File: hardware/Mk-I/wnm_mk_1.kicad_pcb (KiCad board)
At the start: 2 copper layers, 96.5 x 66 mm, 122 parts, among them CON1 USB-MICRO-B, SW1 SW_PUSH, SW10 SW_PUSH, SW11 SW_PUSH, SW12 SW_PUSH, SW13 SW_PUSH, SW14 SW_PUSH, SW15 SW_PUSH, SW16 SW_PUSH, SW18 SW_PUSH, SW19 SW_PUSH, SW2 SW_PUSH, SW20 SW_PUSH, SW21 SW_PUSH, SW22 SW_PUSH, SW3 SW_PUSH, SW4 SW_PUSH, SW5 SW_PUSH, SW6 SW_PUSH, SW7 SW_PUSH, SW8 SW_PUSH, SW9 SW_PUSH, U10 STM32_SWD_Connector, U2 MCP73831, U3 BD33IA5, U4 STM32F407VG, U5 SGTL5000, U6 encoder_and_switch, U7 encoder_and_switch, U8 MOLEX_microSD_47219-2001, U9 SSD1306, X1 CRYSTAL

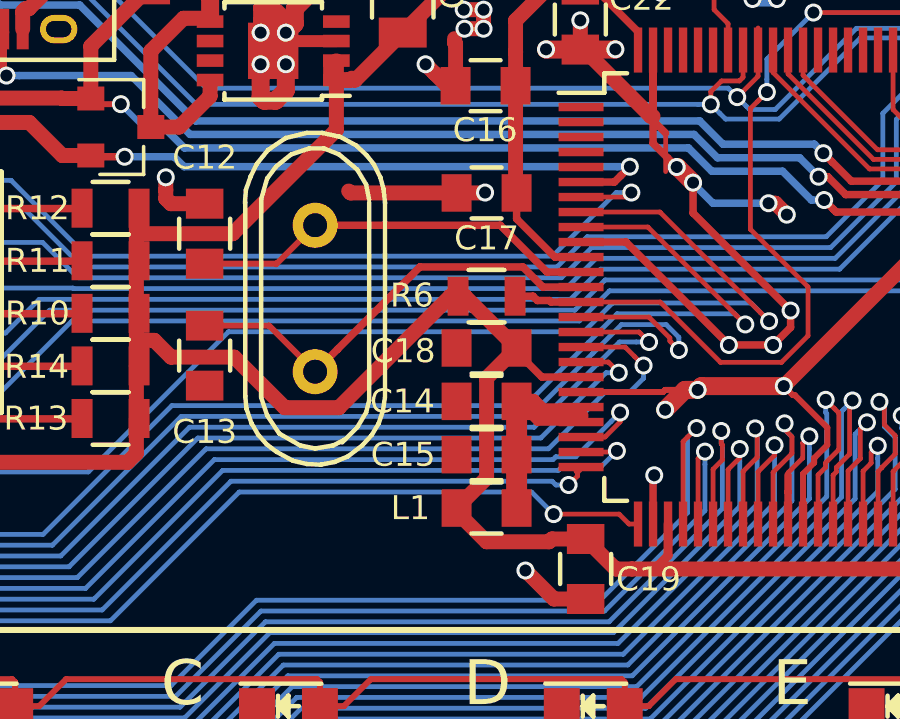
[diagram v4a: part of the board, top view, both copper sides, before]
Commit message: Fix exposed crystal trace by R6 pad mask
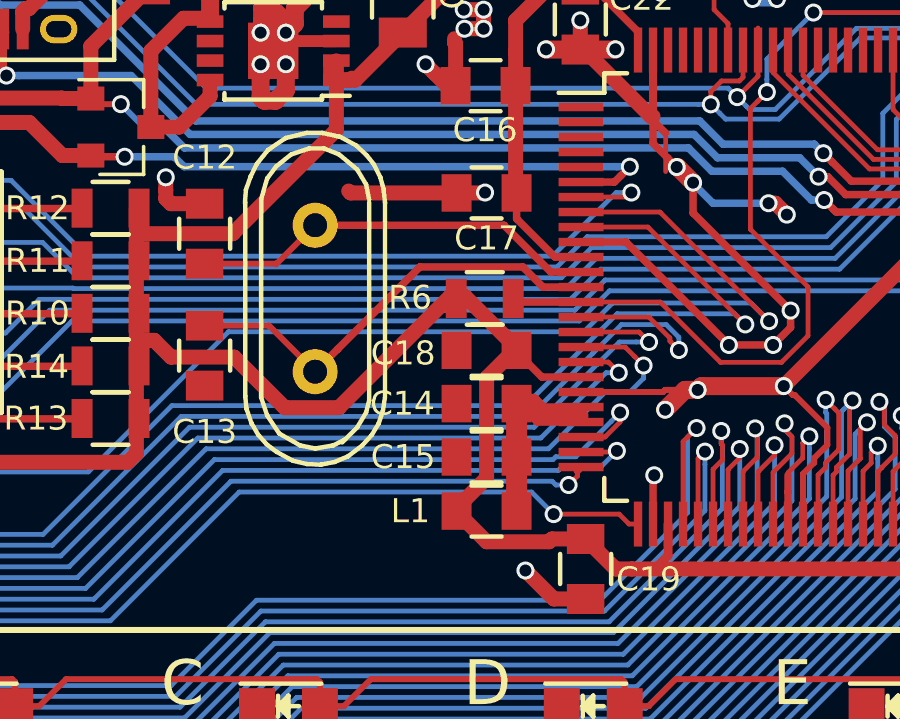
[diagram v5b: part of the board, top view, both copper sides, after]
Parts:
- moved L1 0.10 mm to (145.0, 100.2)
- moved R6 0.10 mm to (145.0, 93.1)
- moved C14 0.08 mm to (145.0, 96.6)
- moved C15 0.08 mm to (145.0, 98.4)
- moved C18 0.08 mm to (145.0, 94.8)
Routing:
- net GND: track 159.0 -> 157.0 mm, vias 56 -> 52
- net (no net): track 0.00 -> 1.93 mm, vias 0 -> 4
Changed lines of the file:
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@@
   (general
     (links 336)
-    (no_connects 1)
+    (no_connects 0)
     (area 79.934999 78.664999 176.605001 144.855001)
     (thickness 1.6)
     (drawings 96)
-    (tracks 2008)
+    (tracks 2005)
     (zones 0)
     (modules 122)
@@
   )
   (setup
-    (last_trace_width 0.5)
+    (last_trace_width 0.25)
     (user_trace_width 0.16)
     (user_trace_width 0.2)
@@
   )
   (module Capacitors_SMD:C_0805 (layer F.Cu)
-    (at 145.034 96.52)
+    (at 145.034 96.5962)
     (descr "Capacitor SMD 0805, reflow soldering, AVX (see smccp.pdf)")
     (tags "capacitor 0805")
@@
   )
   (module Capacitors_SMD:C_0805 (layer F.Cu)
-    (at 145.034 98.298)
+    (at 145.034 98.3742)
     (descr "Capacitor SMD 0805, reflow soldering, AVX (see smccp.pdf)")
     (tags "capacitor 0805")
@@
   )
   (module Capacitors_SMD:C_0805 (layer F.Cu)
-    (at 145.034 94.742)
+    (at 145.034 94.8182)
     (descr "Capacitor SMD 0805, reflow soldering, AVX (see smccp.pdf)")
     (tags "capacitor 0805")
@@
   )
   (module Capacitors_SMD:C_0805 (layer F.Cu)
-    (at 145.034 100.076)
+    (at 145.034 100.1776)
     (descr "Capacitor SMD 0805, reflow soldering, AVX (see smccp.pdf)")
     (tags "capacitor 0805")
@@
   )
   (module Resistors_SMD:R_0805 (layer F.Cu)
-    (at 145.034 93.0148 180)
+    (at 144.973 93.091 180)
     (descr "Resistor SMD 0805, reflow soldering, Vishay (see dcrcw.pdf)")
     (tags "resistor 0805")
@@
     (effects (font (size 1.5 1.5) (thickness 0.3)))
   )
+  (segment (start 144.9324 84.0994) (end 144.2974 84.0994) (width 0.5) (layer F.Cu) (net 0))
+  (via (at 144.2974 84.0994) (size 0.6) (drill 0.4) (layers F.Cu B.Cu) (net 0))
+  (segment (start 144.9324 83.4644) (end 144.9324 84.0994) (width 0.5) (layer F.Cu) (net 0))
+  (via (at 144.9324 84.0994) (size 0.6) (drill 0.4) (layers F.Cu B.Cu) (net 0))
+  (segment (start 144.9324 83.4644) (end 144.272 83.4644) (width 0.5) (layer F.Cu) (net 0))
+  (via (at 144.272 83.4644) (size 0.6) (drill 0.4) (layers F.Cu B.Cu) (net 0))
+  (via (at 144.9324 83.4644) (size 0.6) (drill 0.4) (layers F.Cu B.Cu) (net 0))
   (segment (start 86.512398 109.47118) (end 95.820601 100.162977) (width 0.16) (layer B.Cu) (net 1))
   (segment (start 95.820601 100.162977) (end 107.7535 100.162977) (width 0.16) (layer B.Cu) (net 1))
@@
   (via (at 87.20819 121.1834) (size 0.6) (drill 0.4) (layers F.Cu B.Cu) (net 30))
   (segment (start 90.505 121.19) (end 84.755 121.19) (width 0.25) (layer F.Cu) (net 30))
-  (segment (start 144.9324 84.0994) (end 144.2974 84.0994) (width 0.5) (layer F.Cu) (net 31))
-  (via (at 144.2974 84.0994) (size 0.6) (drill 0.4) (layers F.Cu B.Cu) (net 31))
-  (segment (start 144.9324 83.4644) (end 144.9324 84.0994) (width 0.5) (layer F.Cu) (net 31))
-  (via (at 144.9324 84.0994) (size 0.6) (drill 0.4) (layers F.Cu B.Cu) (net 31))
-  (segment (start 144.9324 83.4644) (end 144.272 83.4644) (width 0.5) (layer F.Cu) (net 31))
-  (via (at 144.272 83.4644) (size 0.6) (drill 0.4) (layers F.Cu B.Cu) (net 31))
   (segment (start 143.9672 84.5693) (end 143.9672 84.4296) (width 0.5) (layer F.Cu) (net 31))
-  (via (at 144.9324 83.4644) (size 0.6) (drill 0.4) (layers F.Cu B.Cu) (net 31))
   (segment (start 154.432 89.916) (end 154.6606 89.916) (width 0.5) (layer F.Cu) (net 31))
   (segment (start 154.6606 89.916) (end 155.0416 90.297) (width 0.5) (layer F.Cu) (net 31))
@@
   (segment (start 134.792 87.376) (end 135.817 86.351) (width 0.5) (layer F.Cu) (net 42))
   (segment (start 135.817 86.351) (end 135.817 85.921001) (width 0.5) (layer F.Cu) (net 42))
+  (segment (start 146.034 90.43199) (end 146.034 89.267) (width 0.25) (layer F.Cu) (net 45))
+  (segment (start 147.31201 91.71) (end 146.034 90.43199) (width 0.25) (layer F.Cu) (net 45))
+  (segment (start 148.183 91.71) (end 147.31201 91.71) (width 0.25) (layer F.Cu) (net 45))
   (segment (start 119.4816 93.1418) (end 119.181601 92.841801) (width 0.5) (layer F.Cu) (net 45))
   (segment (start 114.726999 92.841801) (end 114.366346 93.202454) (width 0.5) (layer F.Cu) (net 45))
@@
   (via (at 119.4816 93.1418) (size 0.6) (drill 0.4) (layers F.Cu B.Cu) (net 45))
   (via (at 122.1486 93.1926) (size 0.6) (drill 0.4) (layers F.Cu B.Cu) (net 45))
-  (segment (start 148.183 91.71) (end 147.308424 91.71) (width 0.25) (layer F.Cu) (net 45))
-  (segment (start 147.308424 91.71) (end 146.034 90.435576) (width 0.25) (layer F.Cu) (net 45))
-  (segment (start 146.034 90.435576) (end 146.034 89.267) (width 0.25) (layer F.Cu) (net 45))
   (segment (start 148.183 91.71) (end 147.587823 91.71) (width 0.25) (layer F.Cu) (net 45))
   (segment (start 166.5986 82.788) (end 166.4736 82.788) (width 0.25) (layer F.Cu) (net 45))
@@
   (segment (start 100.665 125.19) (end 105.075 125.19) (width 0.25) (layer F.Cu) (net 75))
   (segment (start 90.505 125.19) (end 94.915 125.19) (width 0.25) (layer F.Cu) (net 75))
+  (segment (start 139.319 90.65006) (end 145.61566 90.65006) (width 0.25) (layer F.Cu) (net 76))
+  (segment (start 147.1756 92.21) (end 148.31 92.21) (width 0.25) (layer F.Cu) (net 76))
+  (segment (start 145.61566 90.65006) (end 147.1756 92.21) (width 0.25) (layer F.Cu) (net 76))
   (segment (start 138.02106 91.948) (end 138.00506 91.932) (width 0.2) (layer F.Cu) (net 76))
   (segment (start 138.00506 91.932) (end 135.636 91.932) (width 0.2) (layer F.Cu) (net 76))
   (segment (start 139.319 90.65006) (end 138.02106 91.948) (width 0.2) (layer F.Cu) (net 76))
-  (segment (start 139.319 90.65006) (end 145.48866 90.65006) (width 0.25) (layer F.Cu) (net 76))
-  (segment (start 145.48866 90.65006) (end 147.0486 92.21) (width 0.25) (layer F.Cu) (net 76))
-  (segment (start 147.0486 92.21) (end 148.31 92.21) (width 0.25) (layer F.Cu) (net 76))
   (segment (start 139.60094 90.932) (end 139.319 90.65006) (width 0.25) (layer F.Cu) (net 76))
+  (segment (start 146.91219 92.71) (end 146.241989 92.039799) (width 0.25) (layer F.Cu) (net 77))
   (segment (start 137.78306 93.996) (end 135.636 93.996) (width 0.2) (layer F.Cu) (net 77))
   (segment (start 139.319 95.53194) (end 137.78306 93.996) (width 0.2) (layer F.Cu) (net 77))
@@
   (segment (start 146.241989 92.039799) (end 142.811141 92.039799) (width 0.25) (layer F.Cu) (net 77))
   (segment (start 148.31 92.71) (end 146.91219 92.71) (width 0.25) (layer F.Cu) (net 77))
-  (segment (start 146.91219 92.71) (end 146.241989 92.039799) (width 0.25) (layer F.Cu) (net 77))
   (segment (start 147.066 97.0026) (end 148.183 97.0026) (width 0.5) (layer F.Cu) (net 78))
   (segment (start 146.5834 96.52) (end 147.066 97.0026) (width 0.5) (layer F.Cu) (net 78))
@@
   (segment (start 110.55 104.85) (end 110.55 101.982) (width 0.25) (layer F.Cu) (net 125))
   (segment (start 110.55 101.982) (end 110.551 101.981) (width 0.25) (layer F.Cu) (net 125))
+  (segment (start 148.183 93.21) (end 146.042 93.21) (width 0.25) (layer F.Cu) (net 126))
+  (segment (start 146.042 93.21) (end 145.923 93.091) (width 0.25) (layer F.Cu) (net 126))
   (segment (start 155.929017 83.560194) (end 158.903008 83.560194) (width 0.16) (layer F.Cu) (net 126))
   (segment (start 160.7693 80.943755) (end 160.7693 80.519491) (width 0.16) (layer F.Cu) (net 126))
   (segment (start 158.903008 83.560194) (end 160.7693 81.693902) (width 0.16) (layer F.Cu) (net 126))
   (segment (start 160.7693 81.693902) (end 160.7693 80.943755) (width 0.16) (layer F.Cu) (net 126))
-  (segment (start 148.183 93.21) (end 147.183 93.21) (width 0.25) (layer F.Cu) (net 126))
-  (segment (start 147.183 93.21) (end 147.13301 93.16001) (width 0.25) (layer F.Cu) (net 126))
-  (segment (start 147.13301 93.16001) (end 146.72579 93.16001) (width 0.25) (layer F.Cu) (net 126))
-  (segment (start 146.72579 93.16001) (end 146.58058 93.0148) (width 0.25) (layer F.Cu) (net 126))
-  (segment (start 146.58058 93.0148) (end 145.984 93.0148) (width 0.25) (layer F.Cu) (net 126))
   (segment (start 154.077343 86.511698) (end 154.377342 86.211699) (width 0.16) (layer F.Cu) (net 126))
   (segment (start 155.929017 83.560194) (end 154.377342 85.111869) (width 0.16) (layer B.Cu) (net 126))

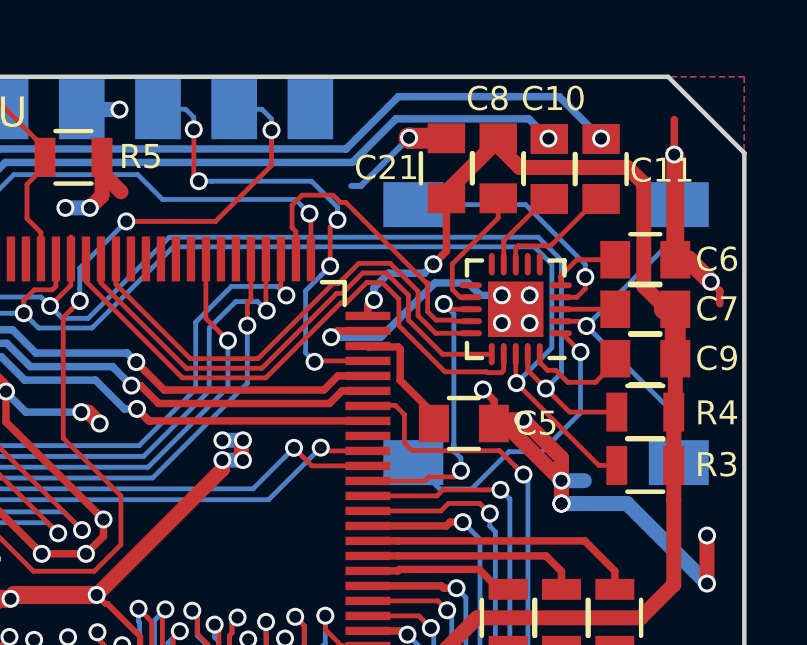
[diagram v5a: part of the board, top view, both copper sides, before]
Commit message: HW: Fix DAC coupling caps
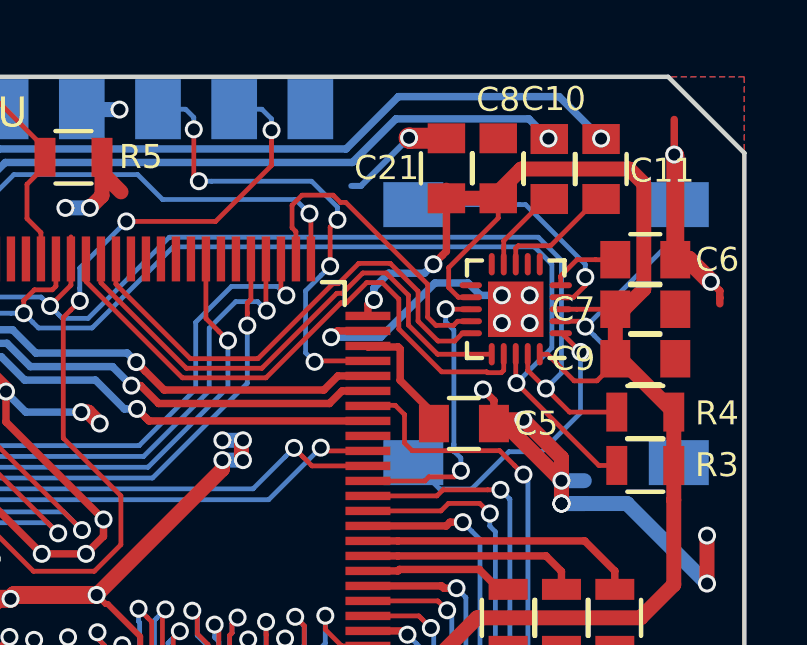
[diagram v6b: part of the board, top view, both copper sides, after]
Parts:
- C12, C13: value C -> 22pF
- C30, C31, C32, C33: value 0,1uF -> 0.1uF
- R15: value R -> 68k
- R7, R8, R9: value R -> 330
- turned C7 to 0 degrees
- turned C8 to 90 degrees
- turned C9 to 0 degrees
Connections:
- C7 pad 2: Net-(C7-Pad2) -> GND
- C8 pad 2: Net-(C8-Pad2) -> GND
- C9 pad 2: Net-(C9-Pad2) -> GND
- U5 pad 12: Net-(C8-Pad2) -> 3V3
- U5 pad 20: Net-(C9-Pad2) -> 3V3
- U5 pad 3: Net-(C7-Pad2) -> 3V3
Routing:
- net 3V3: track 217.8 -> 226.9 mm
- net Net-(C8-Pad2): track 4.40 -> 0.00 mm
- net Net-(C9-Pad2): track 3.47 -> 0.00 mm
- net Net-(C7-Pad2): track 1.82 -> 0.00 mm

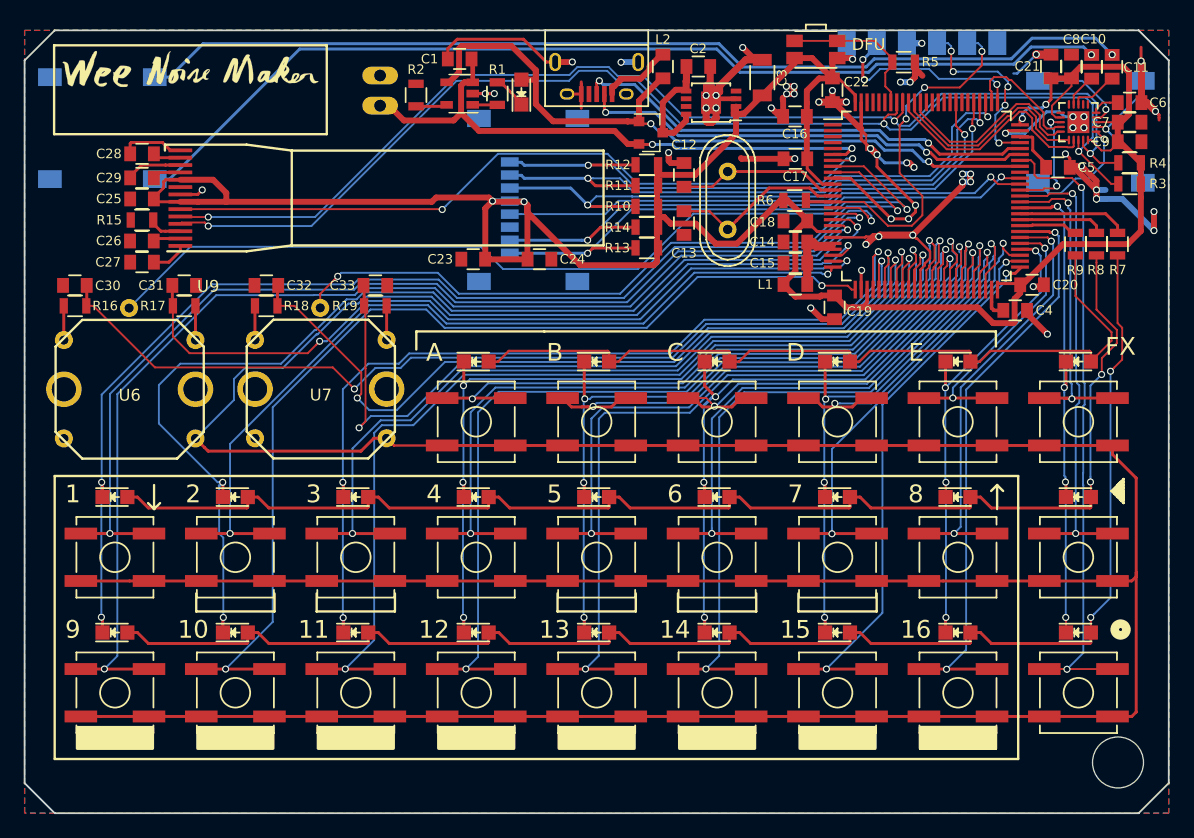
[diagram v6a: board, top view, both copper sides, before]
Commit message: HW: Improve ground layout
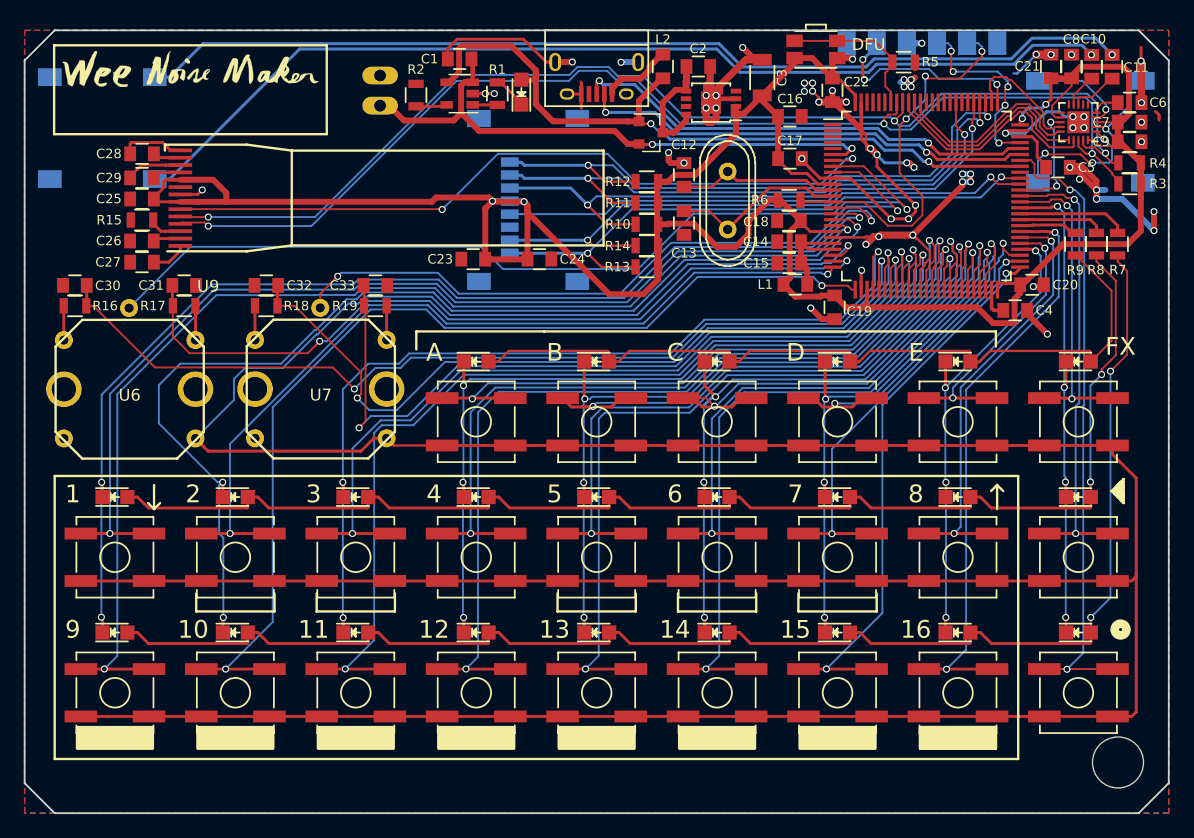
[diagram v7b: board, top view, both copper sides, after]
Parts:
- moved R13 1.61 mm to (132.5, 98.7)
- moved R14 1.56 mm to (132.5, 96.9)
- moved R10 1.51 mm to (132.5, 95.1)
- moved R11 1.47 mm to (132.5, 93.3)
- moved R12 1.42 mm to (132.5, 91.5)
- moved C18 0.54 mm to (144.5, 94.8)
- moved C14 0.53 mm to (144.5, 96.6)
- moved C15 0.52 mm to (144.5, 98.4)
- moved R6 0.46 mm to (144.5, 93.1)
- moved C17 0.46 mm to (144.6, 89.6), turned to 180 degrees
- moved C16 0.43 mm to (144.6, 86.0), turned to 180 degrees
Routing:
- net GND: track 157.0 -> 152.4 mm, vias 52 -> 62
- net Net-(HP_OUT1-Pad3): track 9.94 -> 12.0 mm, vias 1 -> 3
- net Net-(C14-Pad2): track 11.6 -> 9.51 mm
- net (no net): track 1.93 -> 0.00 mm, vias 4 -> 0
- net NRST: track 32.1 -> 33.1 mm
- net SD_CMD: track 49.4 -> 50.3 mm
- net 3V3: track 226.9 -> 227.6 mm
- net SD_DAT3: track 50.1 -> 50.8 mm
- net SD_DAT2: track 50.5 -> 51.2 mm

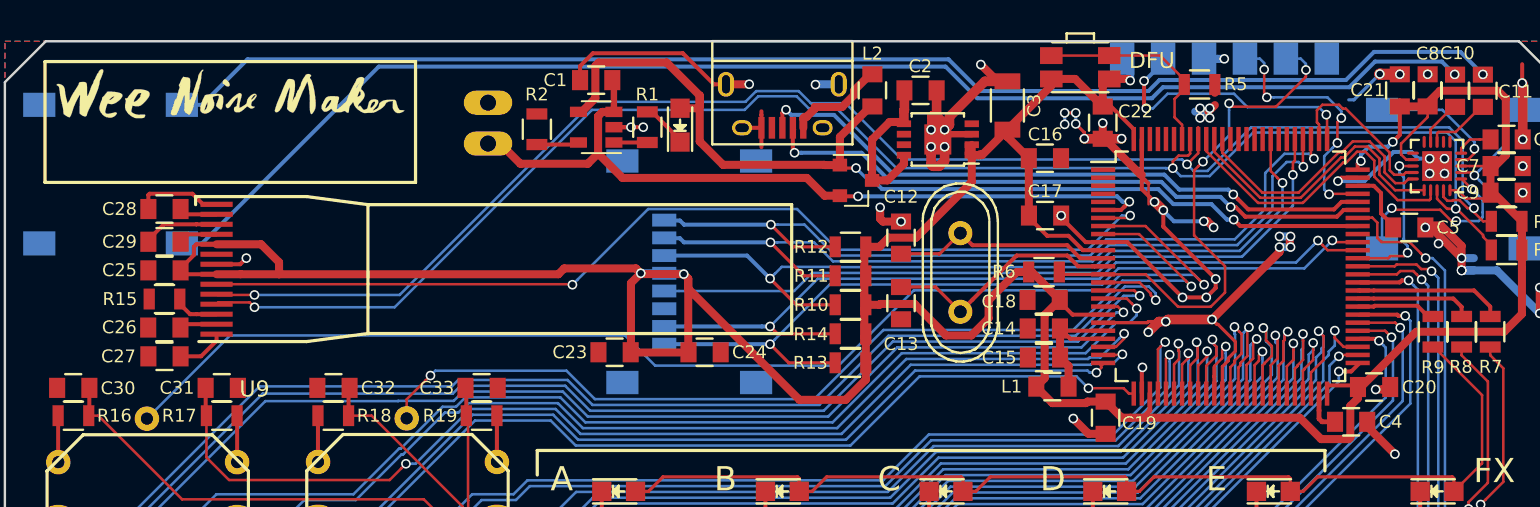
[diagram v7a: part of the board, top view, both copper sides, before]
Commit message: HW: Fix regulator footprint
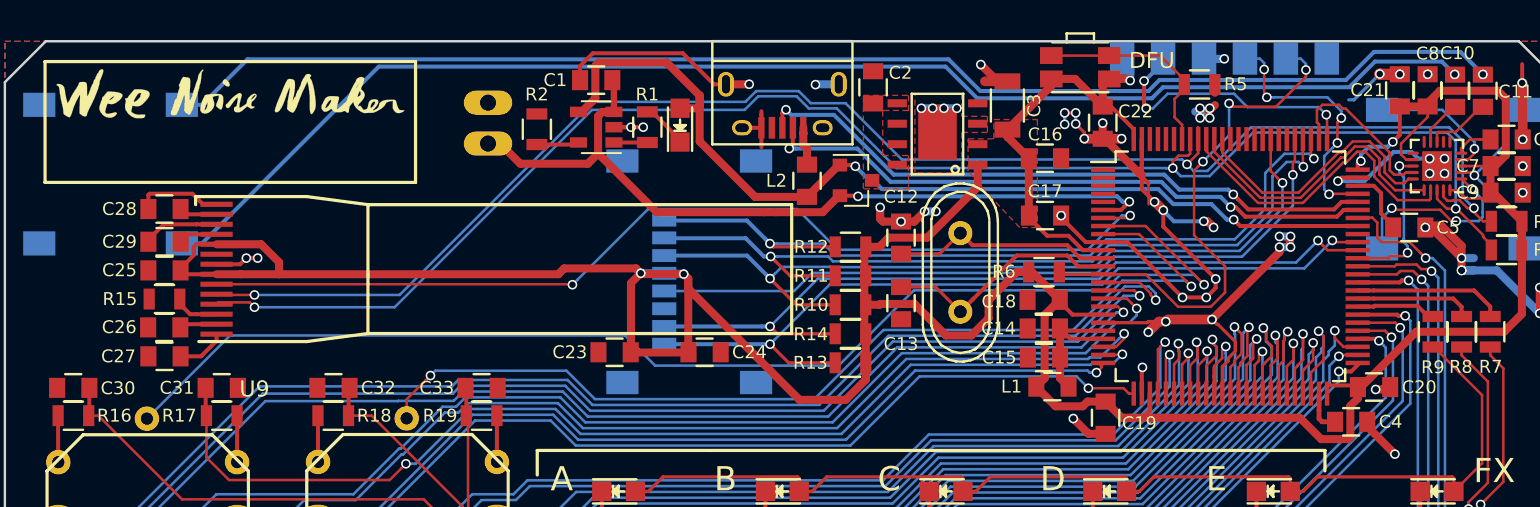
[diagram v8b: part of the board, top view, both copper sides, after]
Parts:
- U3: footprint Housings_SSOP:MSOP-8-1EP_3x3mm_Pitch0.65mm -> POSS:HTSOP-J8
- moved L2 6.93 mm to (129.8, 87.4)
- moved C2 2.95 mm to (133.9, 81.6), turned to 90 degrees
- moved U3 2.93 mm to (140.4, 86.4)
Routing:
- net GND: track 152.4 -> 141.6 mm, vias 62 -> 60
- net VIN: track 9.73 -> 0.00 mm
- net 3V3: track 227.6 -> 223.1 mm
- net Net-(CON1-Pad1): track 6.23 -> 2.39 mm
- net (no net): track 0.00 -> 3.44 mm, vias 0 -> 4
- net VBUS: track 63.2 -> 60.6 mm
- net VBAT: track 49.2 -> 50.1 mm
- added copper zone on F.Cu, net 3V3
- added copper zone on F.Cu, net VIN
